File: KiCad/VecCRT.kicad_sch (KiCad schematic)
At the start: 75 parts, among them J1 RaspiGPIO, J2 K2, J3 Conn_01x03, J4 Conn_01x06, J5 Conn_01x03, J6 Conn_01x06, J7 K2, Q1 2N7000, Q10 2N7000, Q2 2N7002, Q3 2N7002, Q4 2N7000, Q9 2N7000, U1 MCP4822, U2 4066, U3 4066, U4 TL072, U5 TL072, U6 4011, U7 40106, U8 4011

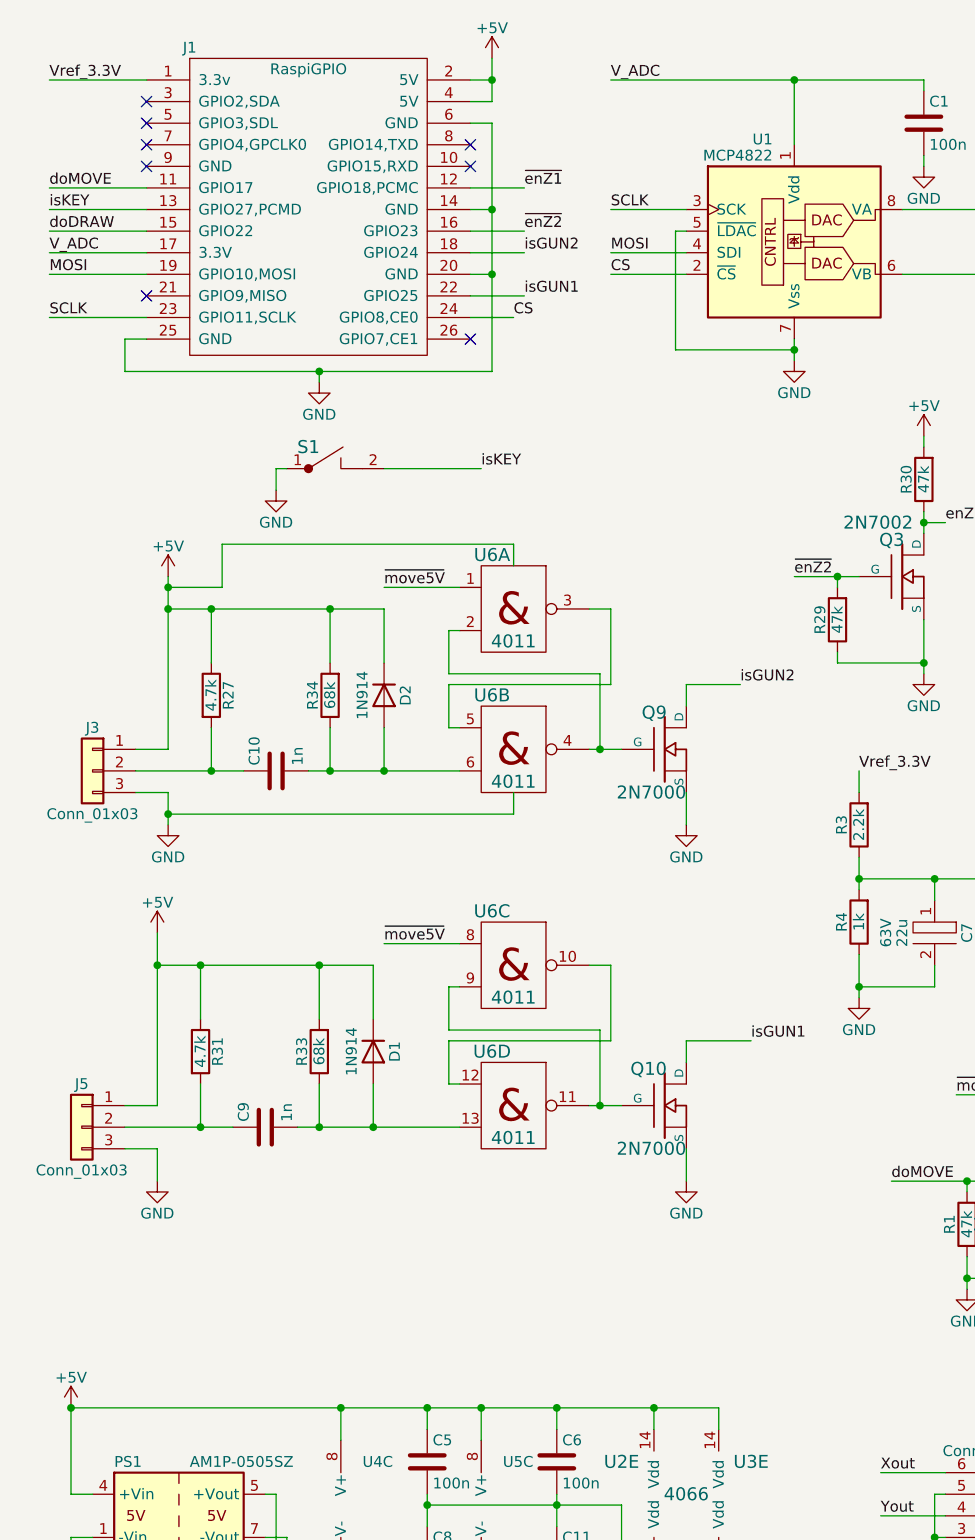
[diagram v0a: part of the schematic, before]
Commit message: new one-shot light-gun
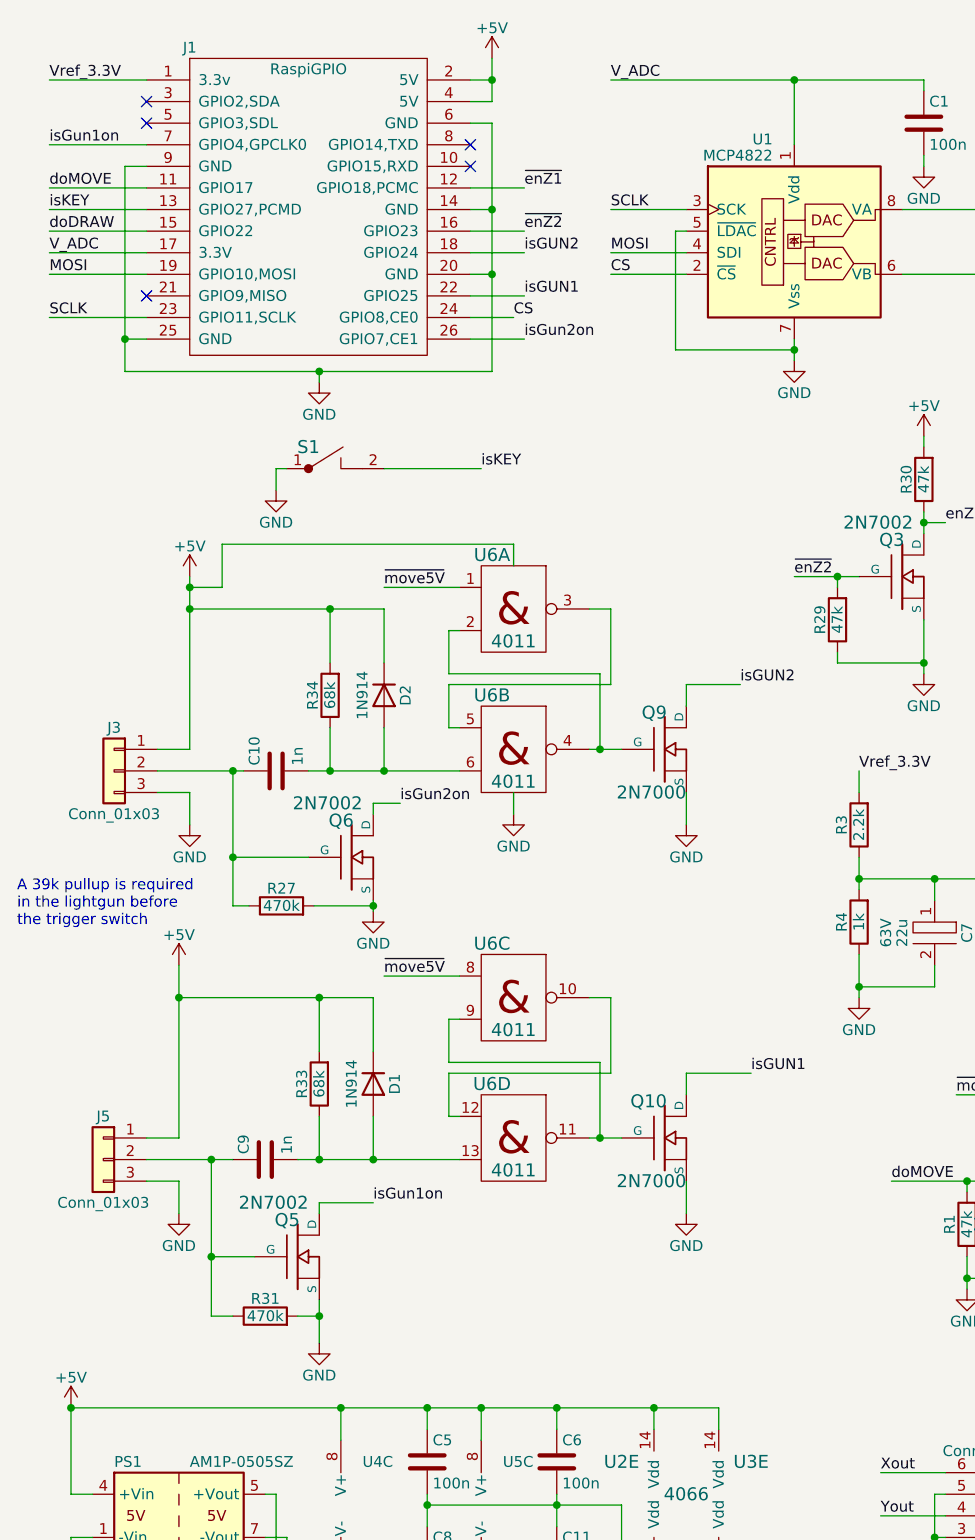
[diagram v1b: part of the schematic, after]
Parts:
- added Q5, Q6: 2N7002, RG:SOT-23_GDS, symbol rg:2N7002
- C1, C11, C5, C6, C8, R1, R2, R23, R26, R29, R30: footprint (none) -> RG:SM-1206B
- C10, C2, C3, C4, C9: footprint (none) -> RG:C2-2
- C7: footprint (none) -> RG:C2-7
- H1, H2, H3, H4: footprint (none) -> MountingHole:MountingHole_3.2mm_M3
- J3, J5: footprint (none) -> RG:PSS_3
- J4, J6: footprint (none) -> RG:PSS_6
- R10, R11, R12, R13, R14, R15, R16, R17, R18, R19, R20, R21, R22, R24, R25, R28, R3, R32, R33, R34, R4, R5, R6, R7, R8, R9: footprint (none) -> RG:R4-2
- R27, R31: value 4.7k -> 470k; footprint (none) -> RG:SM-1206B
- S1: footprint (none) -> RG:Tast-DT6
- U1, U4, U5: footprint (none) -> RG:DIP-8_300
- U2, U3, U6, U8: footprint (none) -> RG:DIP-14_W7.62mm_LongPads
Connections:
- net +5V: no longer R27.1, R31.1
- net GND: now also J1.9 (GND), R27.2, R31.2, Q5.S, Q6.S
- net isGun2on: now reaches J1.26 (GPIO7,CE1)
- net isGun2on: now also Q6.D
- net isGun1on: now reaches J1.7 (GPIO4,GPCLK0)
- net isGun1on: now also Q5.D
- net at C10.1, J3.2 (Pin_2): now also R27.1, Q6.G; no longer R27.2
- net at C9.1, J5.2 (Pin_2): now also R31.1, Q5.G; no longer R31.2
- no-connect marks 8 -> 5
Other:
- note added: "A 39k pullup is required in the lightgun before the trigger switch"
- moved on the sheet: C9, D1, J3, J5, Q10, R27, R31, R33, U6C, U6D

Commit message: minor changes
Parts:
- added C?: 220u, RG:C2-7, symbol rg:ELKO
- R8: value 47k -> 6.8k
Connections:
- net +5V: now also C?.1
- net GND: now also C?.2
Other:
- moved on the sheet: J4
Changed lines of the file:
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@@
   (junction (at 125.73 71.12) (diameter 0) (color 0 0 0 0)
   )
-  (junction (at 110.49 187.96) (diameter 0) (color 0 0 0 0)
+  (junction (at 123.19 187.96) (diameter 0) (color 0 0 0 0)
   )
   (junction (at 57.15 196.85) (diameter 0) (color 0 0 0 0)
@@
   (junction (at 114.3 146.05) (diameter 0) (color 0 0 0 0)
   )
-  (junction (at 110.49 193.04) (diameter 0) (color 0 0 0 0)
+  (junction (at 123.19 193.04) (diameter 0) (color 0 0 0 0)
   )
   (junction (at 251.46 137.16) (diameter 0) (color 0 0 0 0)
@@
   (junction (at 175.26 151.13) (diameter 0) (color 0 0 0 0)
   )
-  (junction (at 220.98 102.87) (diameter 0) (color 0 0 0 0)
-  )
   (junction (at 247.65 39.37) (diameter 0) (color 0 0 0 0)
   )
   (junction (at 38.1 124.46) (diameter 0) (color 0 0 0 0)
   )
+  (junction (at 85.09 196.85) (diameter 0) (color 0 0 0 0)
+  )
   (junction (at 177.8 69.85) (diameter 0) (color 0 0 0 0)
   )
@@
   (junction (at 251.46 154.94) (diameter 0) (color 0 0 0 0)
   )
+  (junction (at 85.09 172.72) (diameter 0) (color 0 0 0 0)
+  )
   (junction (at 135.89 81.28) (diameter 0) (color 0 0 0 0)
   )
@@
     (stroke (width 0.3048) (type default) (color 0 0 0 0))
   )
-  (wire (pts (xy 110.49 182.88) (xy 110.49 187.96))
+  (wire (pts (xy 123.19 182.88) (xy 123.19 187.96))
     (stroke (width 0.3048) (type default) (color 0 0 0 0))
   )
@@
     (stroke (width 0.3048) (type default) (color 0 0 0 0))
   )
-  (wire (pts (xy 220.98 102.87) (xy 223.52 102.87))
-    (stroke (width 0.3048) (type default) (color 0 0 0 0))
-  )
   (wire (pts (xy 196.85 96.52) (xy 196.85 107.95))
     (stroke (width 0.3048) (type default) (color 0 0 0 0))
@@
     (stroke (width 0.3048) (type default) (color 0 0 0 0))
   )
-  (wire (pts (xy 104.14 180.34) (xy 111.76 180.34))
+  (wire (pts (xy 116.84 180.34) (xy 124.46 180.34))
     (stroke (width 0.3048) (type default) (color 0 0 0 0))
   )
@@
     (stroke (width 0.3048) (type default) (color 0 0 0 0))
   )
-  (wire (pts (xy 110.49 193.04) (xy 111.76 193.04))
+  (wire (pts (xy 123.19 193.04) (xy 124.46 193.04))
     (stroke (width 0.3048) (type default) (color 0 0 0 0))
   )
@@
     (stroke (width 0.3048) (type default) (color 0 0 0 0))
   )
-  (wire (pts (xy 111.76 185.42) (xy 104.14 185.42))
+  (wire (pts (xy 124.46 185.42) (xy 116.84 185.42))
     (stroke (width 0.3048) (type default) (color 0 0 0 0))
   )
@@
     (stroke (width 0.3048) (type default) (color 0 0 0 0))
   )
+  (wire (pts (xy 97.79 182.245) (xy 97.79 172.72))
+    (stroke (width 0) (type default) (color 0 0 0 0))
+  )
   (wire (pts (xy 234.95 22.86) (xy 240.03 22.86))
     (stroke (width 0.3048) (type default) (color 0 0 0 0))
@@
     (stroke (width 0.3048) (type default) (color 0 0 0 0))
   )
+  (wire (pts (xy 97.79 196.85) (xy 85.09 196.85))
+    (stroke (width 0) (type default) (color 0 0 0 0))
+  )
   (wire (pts (xy 196.85 22.86) (xy 213.36 22.86))
     (stroke (width 0.3048) (type default) (color 0 0 0 0))
@@
     (stroke (width 0.3048) (type default) (color 0 0 0 0))
   )
-  (wire (pts (xy 110.49 196.85) (xy 110.49 193.04))
+  (wire (pts (xy 123.19 196.85) (xy 123.19 193.04))
     (stroke (width 0.3048) (type default) (color 0 0 0 0))
   )
@@
     (stroke (width 0.3048) (type default) (color 0 0 0 0))
   )
-  (wire (pts (xy 104.14 190.5) (xy 111.76 190.5))
+  (wire (pts (xy 116.84 190.5) (xy 124.46 190.5))
     (stroke (width 0.3048) (type default) (color 0 0 0 0))
   )
@@
     (stroke (width 0.3048) (type default) (color 0 0 0 0))
   )
+  (wire (pts (xy 97.79 172.72) (xy 85.09 172.72))
+    (stroke (width 0) (type default) (color 0 0 0 0))
+  )
   (wire (pts (xy 53.34 86.36) (xy 71.12 86.36))
     (stroke (width 0.3048) (type default) (color 0 0 0 0))
   )
-  (wire (pts (xy 111.76 182.88) (xy 110.49 182.88))
+  (wire (pts (xy 124.46 182.88) (xy 123.19 182.88))
     (stroke (width 0.3048) (type default) (color 0 0 0 0))
   )
@@
     (stroke (width 0.3048) (type default) (color 0 0 0 0))
   )
+  (wire (pts (xy 97.79 189.865) (xy 97.79 196.85))
+    (stroke (width 0) (type default) (color 0 0 0 0))
+  )
   (wire (pts (xy 33.02 64.77) (xy 33.02 62.23))
     (stroke (width 0.3048) (type default) (color 0 0 0 0))
@@
     (stroke (width 0.3048) (type default) (color 0 0 0 0))
   )
-  (wire (pts (xy 110.49 187.96) (xy 111.76 187.96))
+  (wire (pts (xy 123.19 187.96) (xy 124.46 187.96))
     (stroke (width 0.3048) (type default) (color 0 0 0 0))
   )
@@
     (stroke (width 0) (type default) (color 0 0 0 0))
   )
-  (wire (pts (xy 110.49 193.04) (xy 110.49 187.96))
+  (wire (pts (xy 123.19 193.04) (xy 123.19 187.96))
     (stroke (width 0.3048) (type default) (color 0 0 0 0))
   )
@@
     (effects (font (size 1.27 1.27)) (justify left bottom))
   )
-  (label "Yout" (at 104.14 185.42 0)
+  (label "Yout" (at 116.84 185.42 0)
     (effects (font (size 1.27 1.27)) (justify left bottom))
   )
@@
     (effects (font (size 1.27 1.27)) (justify left bottom))
   )
-  (label "z1" (at 104.14 190.5 0)
+  (label "z1" (at 116.84 190.5 0)
     (effects (font (size 1.27 1.27)) (justify left bottom))
   )
@@
     (effects (font (size 1.27 1.27)) (justify left bottom))
   )
-  (label "Xout" (at 104.14 180.34 0)
+  (label "Xout" (at 116.84 180.34 0)
     (effects (font (size 1.27 1.27)) (justify left bottom))
   )
@@
     (pin "1")
   )
-  (symbol (lib_id "Connector_Generic:Conn_01x06") (at 116.84 187.96 0) (mirror x) (unit 1)
+  (symbol (lib_id "Connector_Generic:Conn_01x06") (at 129.54 187.96 0) (mirror x) (unit 1)
     (in_bom yes) (on_board yes)
-    (property "Reference" "J4" (id 0) (at 116.84 195.58 0))
-    (property "Value" "Conn_01x06" (id 1) (at 116.84 177.8 0))
-    (property "Footprint" "RG:PSS_6" (id 2) (at 116.84 187.96 0)
+    (property "Reference" "J4" (id 0) (at 129.54 195.58 0))
+    (property "Value" "Conn_01x06" (id 1) (at 129.54 177.8 0))
+    (property "Footprint" "RG:PSS_6" (id 2) (at 129.54 187.96 0)
       (effects (font (size 1.27 1.27)) hide)
     )
-    (property "Datasheet" "~" (id 3) (at 116.84 187.96 0)
+    (property "Datasheet" "~" (id 3) (at 129.54 187.96 0)
       (effects (font (size 1.27 1.27)) hide)
     )
@@
     (in_bom yes) (on_board yes)
     (property "Reference" "R8" (id 0) (at 182.118 132.08 90))
-    (property "Value" "47k" (id 1) (at 184.15 132.08 90))
+    (property "Value" "6.8k" (id 1) (at 184.15 132.08 90))
     (property "Footprint" "RG:R4-2" (id 2) (at 185.928 132.08 90)
       (effects (font (size 1.27 1.27)) hide)
@@
     (pin "3")
   )
-  (symbol (lib_id "power:GND") (at 110.49 196.85 0) (unit 1)
+  (symbol (lib_id "power:GND") (at 123.19 196.85 0) (unit 1)
     (in_bom yes) (on_board yes)
-    (property "Reference" "#PWR025" (id 0) (at 110.49 203.2 0)
+    (property "Reference" "#PWR025" (id 0) (at 123.19 203.2 0)
       (effects (font (size 1.27 1.27)) hide)
     )
-    (property "Value" "GND" (id 1) (at 110.49 200.66 0))
-    (property "Footprint" "" (id 2) (at 110.49 196.85 0)
+    (property "Value" "GND" (id 1) (at 123.19 200.66 0))
+    (property "Footprint" "" (id 2) (at 123.19 196.85 0)
       (effects (font (size 1.27 1.27)) hide)
     )
-    (property "Datasheet" "" (id 3) (at 110.49 196.85 0)
+    (property "Datasheet" "" (id 3) (at 123.19 196.85 0)
       (effects (font (size 1.27 1.27)) hide)
     )
@@
     (pin "2")
   )
+  (symbol (lib_id "rg:ELKO") (at 97.79 187.325 270) (unit 1)
+    (in_bom yes) (on_board yes)
+    (property "Reference" "C?" (id 0) (at 101.6 186.055 0))
+    (property "Value" "220u" (id 1) (at 93.98 186.055 0))
+    (property "Footprint" "RG:C2-7" (id 2) (at 97.79 187.325 0)
+      (effects (font (size 1.524 1.524)) hide)
+    )
+    (property "Datasheet" "" (id 3) (at 97.79 187.325 0)
+      (effects (font (size 1.524 1.524)))
+    )
+    (property "Voltage" "6V" (id 4) (at 92.075 186.055 0))
+    (pin "1")
+    (pin "2")
+  )
   (symbol (lib_id "power:GND") (at 60.96 102.87 0) (unit 1)
     (in_bom yes) (on_board yes)
@@
       (reference "C11") (unit 1) (value "100n") (footprint "RG:SM-1206B")
     )
+    (path "/1ca25c26-93d8-469d-96b3-7b05369ae2a4"
+      (reference "C?") (unit 1) (value "220u") (footprint "RG:C2-7")
+    )
     (path "/00000000-0000-0000-0000-0000648bedcb"
       (reference "D1") (unit 1) (value "1N914") (footprint "Diode_THT:D_DO-35_SOD27_P7.62mm_Horizontal")
@@
     )
     (path "/00000000-0000-0000-0000-000064830a2d"
-      (reference "R8") (unit 1) (value "47k") (footprint "RG:R4-2")
+      (reference "R8") (unit 1) (value "6.8k") (footprint "RG:R4-2")
     )
     (path "/00000000-0000-0000-0000-00006453444b"

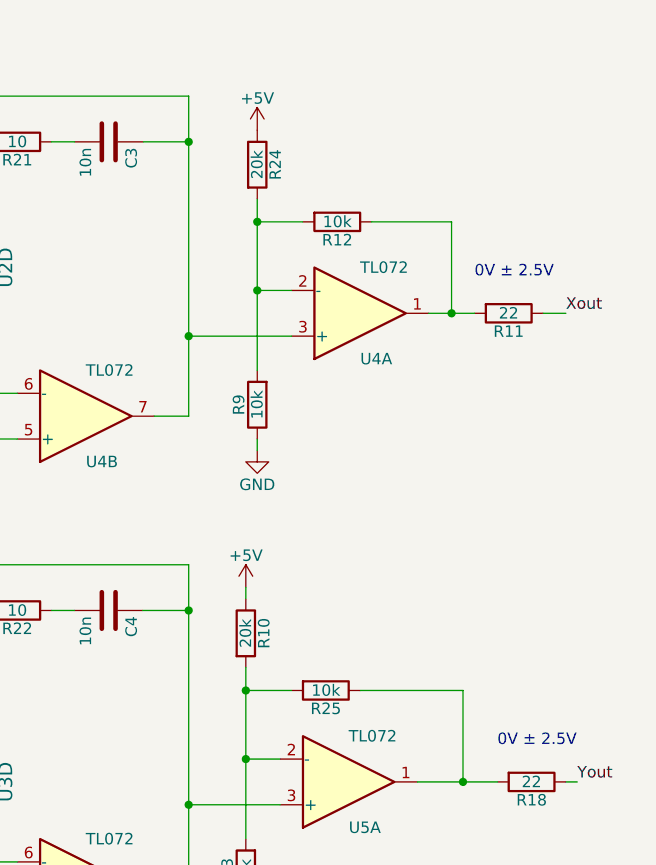
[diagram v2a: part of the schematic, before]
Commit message: Added lightgun for OPL-820
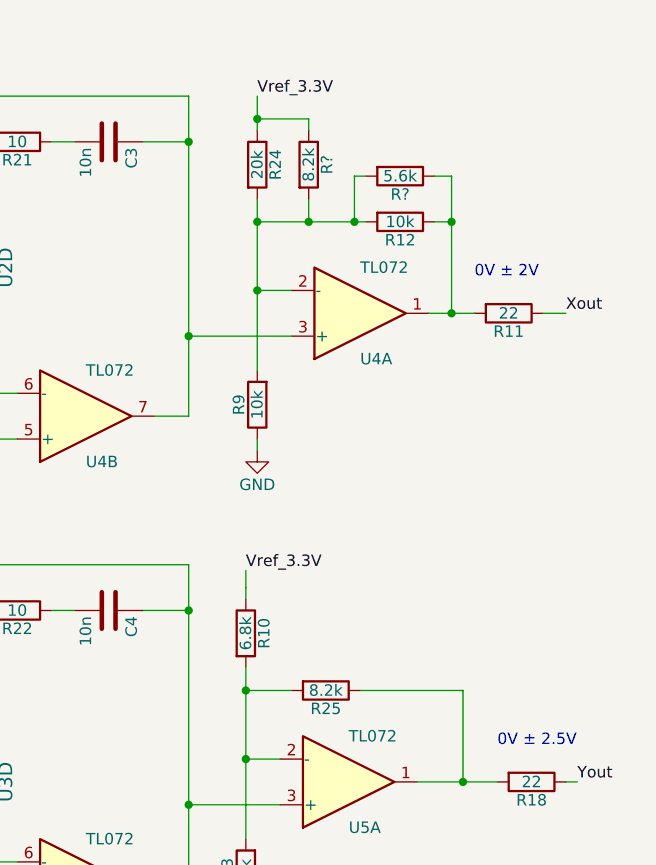
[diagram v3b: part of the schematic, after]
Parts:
- added R?: 8.2k, RG:R4-2, symbol Device:R
- added R?: 5.6k, RG:R4-2, symbol Device:R
- R10: value 20k -> 6.8k
- R25: value 10k -> 8.2k
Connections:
- net +5V: no longer R10.1, R24.1
- net Vref_3.3V: now also R10.1, R24.1, R?.1
- net at R11.2, R12.1, U4.1: now also R?.1
- net at R12.2, R24.2, R9.2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: now also R?.2, R?.2
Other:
- note added: "0V ± 2V"
- moved on the sheet: R12

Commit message: before 1.0
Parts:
- added J8: Conn_01x03, RG:PSS_3, symbol Connector_Generic:Conn_01x03
- added K1: SchEin, PINHEAD1-2, symbol rg:SchEin
- added Q7: 2N7000, RG:FETsgd_inline, symbol rg:BS170
- added R35, R36: 39k, RG:R4-2, symbol Device:R
- added X1: OPL820-OC, symbol rg:OPL820-OC
- gave numbers to parts that had none: 3
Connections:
- net GND: now also J8.3 (Pin_3), Q7.S, X1.1
- new net: K1.1, Q7.D, R36.1
- new net: J8.2 (Pin_2), K1.2
- new net: Q7.G, R35.1, X1.2
- new net: J8.1 (Pin_1), R35.2, R36.2, X1.3
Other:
- note added: "Lightgun"
- moved on the sheet: J4, J6
